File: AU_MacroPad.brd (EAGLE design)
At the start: 59.7 x 104.1 mm, 96 parts, among them IC1 74HCT1G125DBV, IC3 RP2040_QFN56, SW2 RA SW, SW3 EN11-VSM1AF15, U1 W25Q64, U2 RT9080-3.3, U3 PAM8302, X1 TYPE C, X2 ZJY130-2864KSWLG22, Y1 12MHz/12pF

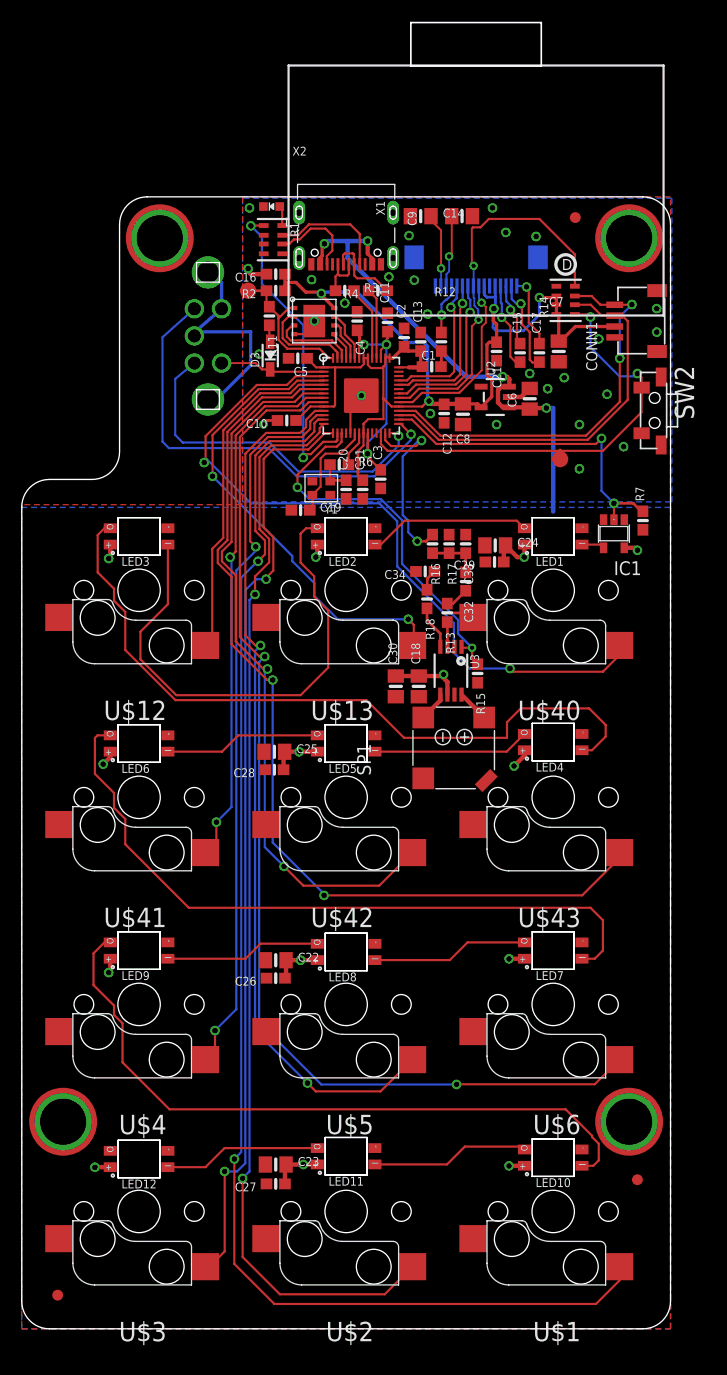
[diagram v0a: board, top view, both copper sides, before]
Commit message: Connector rotated 180 degrees and traces re-routed
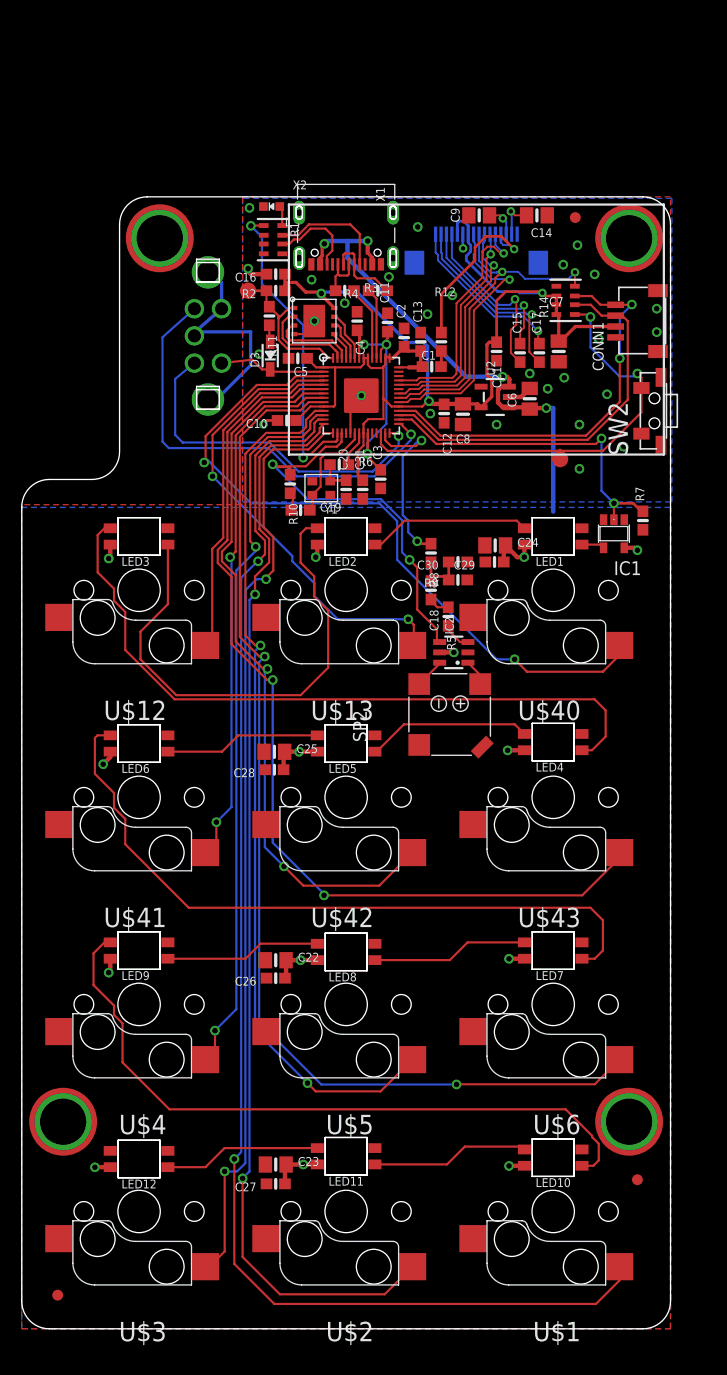
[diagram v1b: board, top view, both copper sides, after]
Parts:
- removed C32, C34: 0.1uF, microbuilder:0603-NO
- removed C33: 10nF, microbuilder:0603-NO
- removed R13, R18: 47K, microbuilder:0603-NO
- removed R15: 10K, microbuilder:0603-NO
- removed R16: 1K, microbuilder:0603-NO
- removed R17: DNP, microbuilder:0603-NO
- removed SP1: 7.5mm SPK, microbuilder:BUZZER_SMT_7.5MM
- removed U$81: (no value), microbuilder:PCBFEAT-REV-040
- removed U3: PAM8302, microbuilder:MSOP8_0.65MM
- added IC2: PAM8301, microbuilder:SOT23-6
- added R10: 10K, microbuilder:0603-NO
- added R5: 47K, microbuilder:0603-NO
- added R8: 1K, microbuilder:0603-NO
- added R9: DNP, microbuilder:0603-NO
- added SP2: 7.5mm SPK, microbuilder:BUZZER_SMT_7.5MM
- C18: value 10uF -> 0.1uF; device microbuilder:0805-NO -> microbuilder:0603-NO
- C19, C20: value 22pF -> 12pF
- C30: value 10uF -> 10nF; device microbuilder:0805-NO -> microbuilder:0603-NO
- C6, C8: value 10uF -> 10µF
- CONN1: device adafruit_electromech:JST_SH4 -> microbuilder:JST_SH4
- R2: value 10K -> 10k
- U1: value W25Q64 -> GD25x16
- U2: value RT9080-3.3 -> AP2112K-3.3; device adafruit_power:SOT23-5 -> microbuilder:SOT23-5
- Y1: value 12MHz/12pF -> 12MHZ
- moved C30 12.8 mm to (40.1, 70.5), turned to 180 degrees
- moved C14 10.7 mm to (47.4, 102.4), turned to 180 degrees
- moved C18 8.91 mm to (37.7, 67.9), turned to 270 degrees
- moved X2 3.11 mm to (41.8, 94.0)
- moved C9 1.58 mm to (42.1, 102.4), turned to 0 degrees
- moved X1 1.27 mm to (29.8, 101.5)
- moved CONN1 0.59 mm to (57.1, 92.7)
- turned SW2 to 90 degrees
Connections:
- removed net IN+: R13.2, U3.3
- removed net IN-: R18.2, U3.4
- removed net N$28: C32.2, R13.1
- removed net N$29: C32.1, C33.2, R16.2, R17.2
- removed net N$30: C34.1, R18.1
- removed net N$31: SP1.-, U3.5
- removed net N$32: SP1.+, U3.8
- new net N$100: C18.1, C30.2, R8.2, R9.2
- new net N$22: IC2.1, SP2.+
- new net N$27: IC2.6, SP2.-
- new net N$8: C18.2, R5.1
- new net N$9: IC2.3, R5.2
- net 5.0V: now also IC2.5; no longer C18.2, C30.2, U3.6
- net GND: now also IC2.2, R10.2, R9.1; no longer C18.1, C33.1, C34.2, R15.2, R17.1, U3.7
- net SPEAKER: now also R8.1; no longer R16.1
- net SPKR_SD: now also IC2.4, R10.1; no longer R15.1, U3.1
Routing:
- net N$21: track 4.74 -> 15.9 mm
- net N$26: track 5.83 -> 15.0 mm
- net N$24: track 6.62 -> 15.6 mm
- net N$23: track 8.73 -> 17.5 mm
- net MOSI: track 13.7 -> 22.3 mm
- net N$25: track 7.99 -> 16.4 mm
- net OLED_CS: track 17.0 -> 25.2 mm
- net 3.3V: track 106.8 -> 113.4 mm, vias 4 -> 3
- net OLED_DC: track 15.3 -> 21.6 mm
- net SCK: track 14.3 -> 20.2 mm
- net 5.0V: track 85.5 -> 80.1 mm
- net N$100: track 0.00 -> 5.21 mm
- net N$29: track 4.81 -> 0.00 mm
- net IN-: track 4.05 -> 0.00 mm
- net OLED_RST: track 35.8 -> 31.9 mm
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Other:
- outline, holes or cut-outs redrawn

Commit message: Add files via upload
Built from Limor's files. Rotated connector 180 degrees and re-routed.
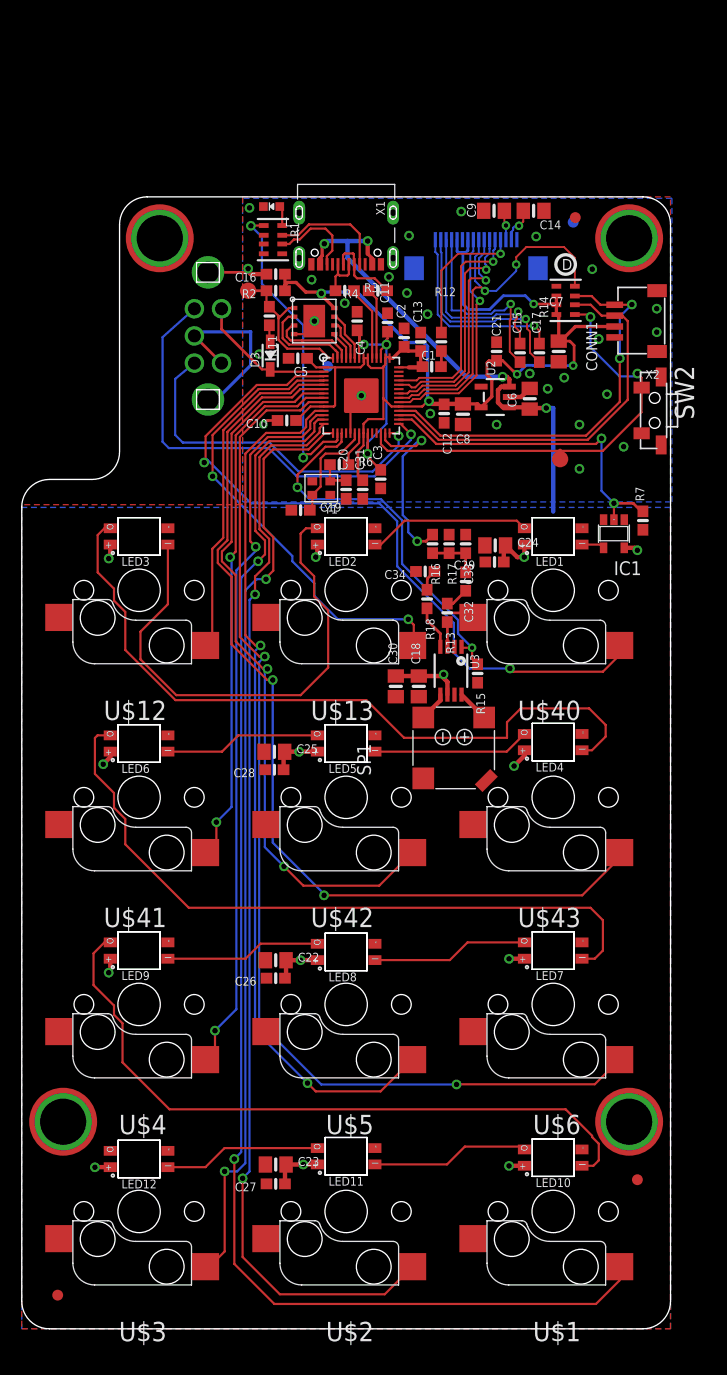
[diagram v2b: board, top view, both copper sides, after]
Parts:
- removed IC2: PAM8301, microbuilder:SOT23-6
- removed R10: 10K, microbuilder:0603-NO
- removed R5: 47K, microbuilder:0603-NO
- removed R8: 1K, microbuilder:0603-NO
- removed R9: DNP, microbuilder:0603-NO
- removed SP2: 7.5mm SPK, microbuilder:BUZZER_SMT_7.5MM
- added C32, C34: 0.1uF, microbuilder:0603-NO
- added C33: 10nF, microbuilder:0603-NO
- added R13, R18: 47K, microbuilder:0603-NO
- added R15: 10K, microbuilder:0603-NO
- added R16: 1K, microbuilder:0603-NO
- added R17: DNP, microbuilder:0603-NO
- added SP1: 7.5mm SPK, microbuilder:BUZZER_SMT_7.5MM
- added U$79, U$83: FIDUCIAL_1MM, microbuilder:FIDUCIAL_1MM
- added U$81: (no value), microbuilder:PCBFEAT-REV-040
- added U3: PAM8302, microbuilder:MSOP8_0.65MM
- C18: value 0.1uF -> 10uF; device microbuilder:0603-NO -> microbuilder:0805-NO
- C19, C20: value 12pF -> 22pF
- C30: value 10nF -> 10uF; device microbuilder:0603-NO -> microbuilder:0805-NO
- C6, C8: value 10µF -> 10uF
- CONN1: device microbuilder:JST_SH4 -> adafruit_electromech:JST_SH4
- R2: value 10k -> 10K
- U1: value GD25x16 -> W25Q64
- U2: value AP2112K-3.3 -> RT9080-3.3; device microbuilder:SOT23-5 -> adafruit_power:SOT23-5
- X2: value ZJY130-2864KSWLG22 -> ZJY130-2864KSWLG22_CONN; device adafruit_display:ZJY130-2864KSWLG22 -> adafruit_display:ZJY130-2864KSWLG22_JUSTCONN
- Y1: value 12MHZ -> 12MHz/12pF
- moved C30 12.8 mm to (34.4, 59.1), turned to 90 degrees
- moved C18 8.91 mm to (36.5, 59.1), turned to 90 degrees
- moved X2 5.08 mm to (41.8, 99.1), turned to 180 degrees
- moved C9 1.43 mm to (43.5, 102.9)
- moved X1 1.27 mm to (29.8, 100.2)
- moved CONN1 0.59 mm to (56.6, 92.7)
- moved C14 0.52 mm to (47.1, 102.9)
- turned SW2 to 270 degrees
- turned C21 to 270 degrees
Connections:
- removed net N$100: C18.1, C30.2, R8.2, R9.2
- removed net N$22: IC2.1, SP2.+
- removed net N$27: IC2.6, SP2.-
- removed net N$8: C18.2, R5.1
- removed net N$9: IC2.3, R5.2
- new net IN+: R13.2, U3.3
- new net IN-: R18.2, U3.4
- new net N$28: C32.2, R13.1
- new net N$29: C32.1, C33.2, R16.2, R17.2
- new net N$30: C34.1, R18.1
- new net N$31: SP1.-, U3.5
- new net N$32: SP1.+, U3.8
- net 5.0V: now also C18.2, C30.2, U3.6; no longer IC2.5
- net GND: now also C18.1, C33.1, C34.2, R15.2, R17.1, SW3.D, U3.7; no longer IC2.2, R10.2, R9.1, SW3.E
- net SPEAKER: now also R16.1; no longer R8.1
- net SPKR_SD: now also R15.1, U3.1; no longer IC2.4, R10.1
- net USBBOOT: now also SW3.E; no longer SW3.D
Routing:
- net 5.0V: track 80.1 -> 85.5 mm
- net N$100: track 5.21 -> 0.00 mm
- net N$29: track 0.00 -> 4.81 mm
- net IN-: track 0.00 -> 4.05 mm
- net OLED_CS: track 25.2 -> 21.3 mm
- net OLED_RST: track 31.9 -> 35.7 mm
- net 3.3V: track 113.4 -> 116.8 mm, vias 3 -> 5
- net USBBOOT: track 9.99 -> 13.0 mm
- net N$32: track 0.00 -> 2.96 mm
- net N$21: track 15.9 -> 13.1 mm
- net N$31: track 0.00 -> 2.75 mm
- net N$27: track 2.74 -> 0.00 mm
- net N$9: track 2.68 -> 0.00 mm
- net N$24: track 15.6 -> 18.2 mm
- net N$22: track 2.43 -> 0.00 mm
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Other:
- outline, holes or cut-outs redrawn
